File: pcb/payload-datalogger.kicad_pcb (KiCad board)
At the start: 2 copper layers, 50.5 x 41.5 mm, 39 parts, among them J1 2.54mm 01x02 header, J2 DE15 Socket, SW2 PTS815, U1 XIAO-ESP32-C3-DIP, U2 NCP177AMX330TCG, U3 W25X40CLSN, U4 MCP96RL00T-E_MX, U5 MCP96RL00T-E_MX, U6 MCP96RL00T-E_MX, U7 MCP96RL00T-E_MX

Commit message: Update payload-datalogger.kicad_pcb
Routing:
- net +3V3: track 18.5 -> 14.1 mm
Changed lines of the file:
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@@
 			(at -4.315 -2.77 90)
 			(layer "F.SilkS")
+			(hide yes)
 			(effects
 				(font
@@
 	)
 	(segment
-		(start 107.5 47.46)
-		(end 110.46 47.46)
-		(width 1)
-		(layer "F.Cu")
-		(net 3)
-	)
-	(segment
 		(start 84.5 67.85)
 		(end 84 67.85)
@@
 		(layer "F.Cu")
 		(net 3)
-	)
-	(segment
-		(start 107.5 47.46)
-		(end 106.04 47.46)
-		(width 1)
-		(layer "F.Cu")
-		(net 3)

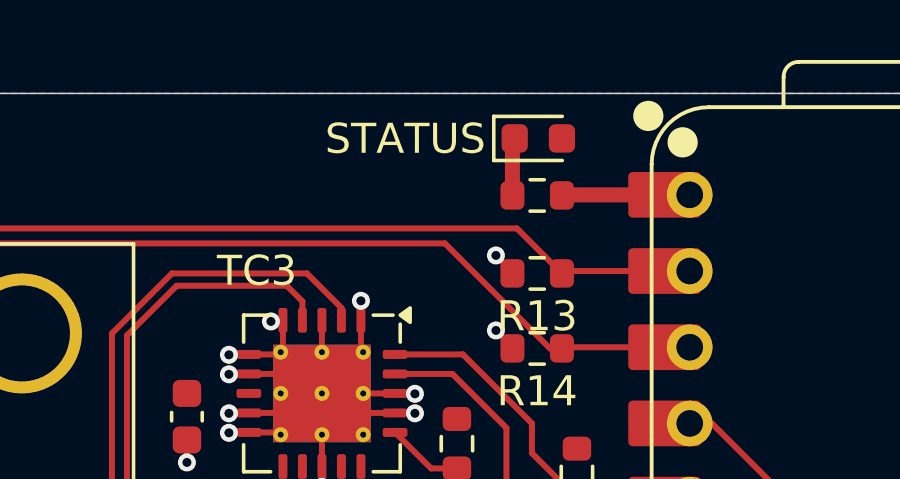
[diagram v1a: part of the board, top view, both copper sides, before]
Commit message: Add user button debounce to sch
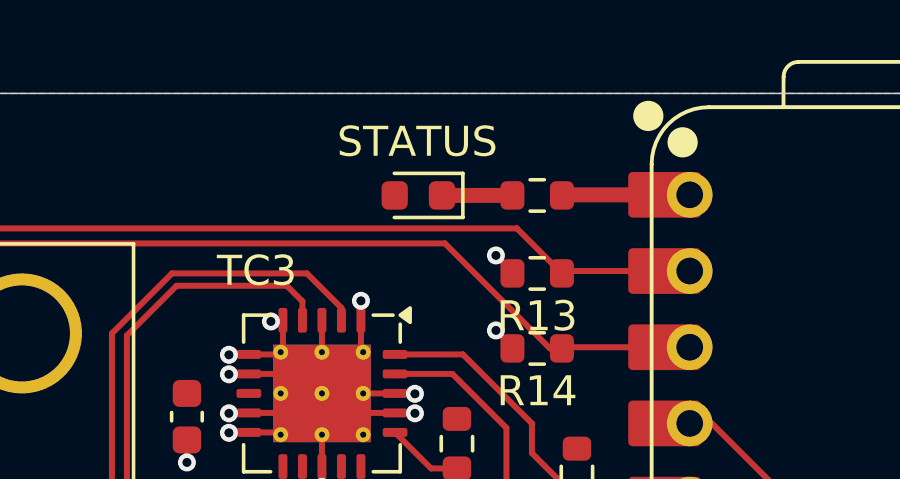
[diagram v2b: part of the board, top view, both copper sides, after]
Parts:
- moved D1 4.43 mm to (83.2, 42.4), turned to 180 degrees
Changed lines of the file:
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@@
 	(footprint "LED_SMD:LED_0603_1608Metric"
 		(layer "F.Cu")
-		(at 87.2125 40.5)
+		(at 83.2125 42.4 180)
 		(descr "LED SMD 0603 (1608 Metric), square (rectangular) end terminal, IPC_7351 nominal, (Body size source: http://www.tortai-tech.com/upload/download/2011102023233369053.pdf), generated with kicad-footprint-generator")
 		(tags "LED")
@@
 		)
 		(property "Datasheet" ""
-			(at 0 0 0)
+			(at 0 0 180)
 			(unlocked yes)
 			(layer "F.Fab")
@@
 		)
 		(property "Description" "Light emitting diode"
-			(at 0 0 0)
+			(at 0 0 180)
 			(unlocked yes)
 			(layer "F.Fab")
@@
 		)
 		(property "Sim.Pins" "1=K 2=A"
-			(at 0 0 0)
+			(at 0 0 180)
 			(unlocked yes)
 			(layer "F.Fab")
@@
 		(attr smd)
 		(fp_line
-			(start -1.485 -0.735)
-			(end -1.485 0.735)
+			(start 0.8 -0.735)
+			(end -1.485 -0.735)
 			(stroke
 				(width 0.12)
@@
 		)
 		(fp_line
-			(start 0.8 -0.735)
-			(end -1.485 -0.735)
+			(start -1.485 -0.735)
+			(end -1.485 0.735)
 			(stroke
 				(width 0.12)
@@
 		)
 		(fp_line
-			(start -1.48 -0.73)
-			(end 1.48 -0.73)
+			(start 1.48 0.73)
+			(end -1.48 0.73)
 			(stroke
 				(width 0.05)
@@
 		)
 		(fp_line
-			(start -1.48 0.73)
-			(end -1.48 -0.73)
+			(start 1.48 -0.73)
+			(end 1.48 0.73)
 			(stroke
 				(width 0.05)
@@
 		)
 		(fp_line
-			(start 1.48 -0.73)
-			(end 1.48 0.73)
+			(start -1.48 0.73)
+			(end -1.48 -0.73)
 			(stroke
 				(width 0.05)
@@
 		)
 		(fp_line
-			(start 1.48 0.73)
-			(end -1.48 0.73)
+			(start -1.48 -0.73)
+			(end 1.48 -0.73)
 			(stroke
 				(width 0.05)
@@
 		)
 		(fp_line
-			(start -0.8 -0.1)
-			(end -0.8 0.4)
+			(start 0.8 0.4)
+			(end 0.8 -0.4)
 			(stroke
 				(width 0.1)
@@
 		)
 		(fp_line
-			(start -0.8 0.4)
-			(end 0.8 0.4)
+			(start 0.8 -0.4)
+			(end -0.5 -0.4)
 			(stroke
 				(width 0.1)
@@
 		)
 		(fp_line
-			(start 0.8 -0.4)
-			(end -0.5 -0.4)
+			(start -0.8 0.4)
+			(end 0.8 0.4)
 			(stroke
 				(width 0.1)
@@
 		)
 		(fp_line
-			(start 0.8 0.4)
-			(end 0.8 -0.4)
+			(start -0.8 -0.1)
+			(end -0.8 0.4)
 			(stroke
 				(width 0.1)
@@
 		)
 		(pad "1" smd roundrect
-			(at -0.7875 0)
+			(at -0.7875 0 180)
 			(size 0.875 0.95)
 			(layers "F.Cu" "F.Mask" "F.Paste")
@@
 		)
 		(pad "2" smd roundrect
-			(at 0.7875 0)
+			(at 0.7875 0 180)
 			(size 0.875 0.95)
 			(layers "F.Cu" "F.Mask" "F.Paste")
@@
 	)
 	(gr_text "STATUS"
-		(at 80.1 41.1 0)
+		(at 80.5 41.2 0)
 		(layer "F.SilkS")
 		(effects
@@
 	)
 	(segment
-		(start 86.35 40.575)
-		(end 86.425 40.5)
-		(width 0.5)
-		(layer "F.Cu")
-		(net 6)
-	)
-	(segment
 		(start 86.35 42.4)
-		(end 86.35 40.575)
+		(end 84 42.4)
 		(width 0.5)
 		(layer "F.Cu")

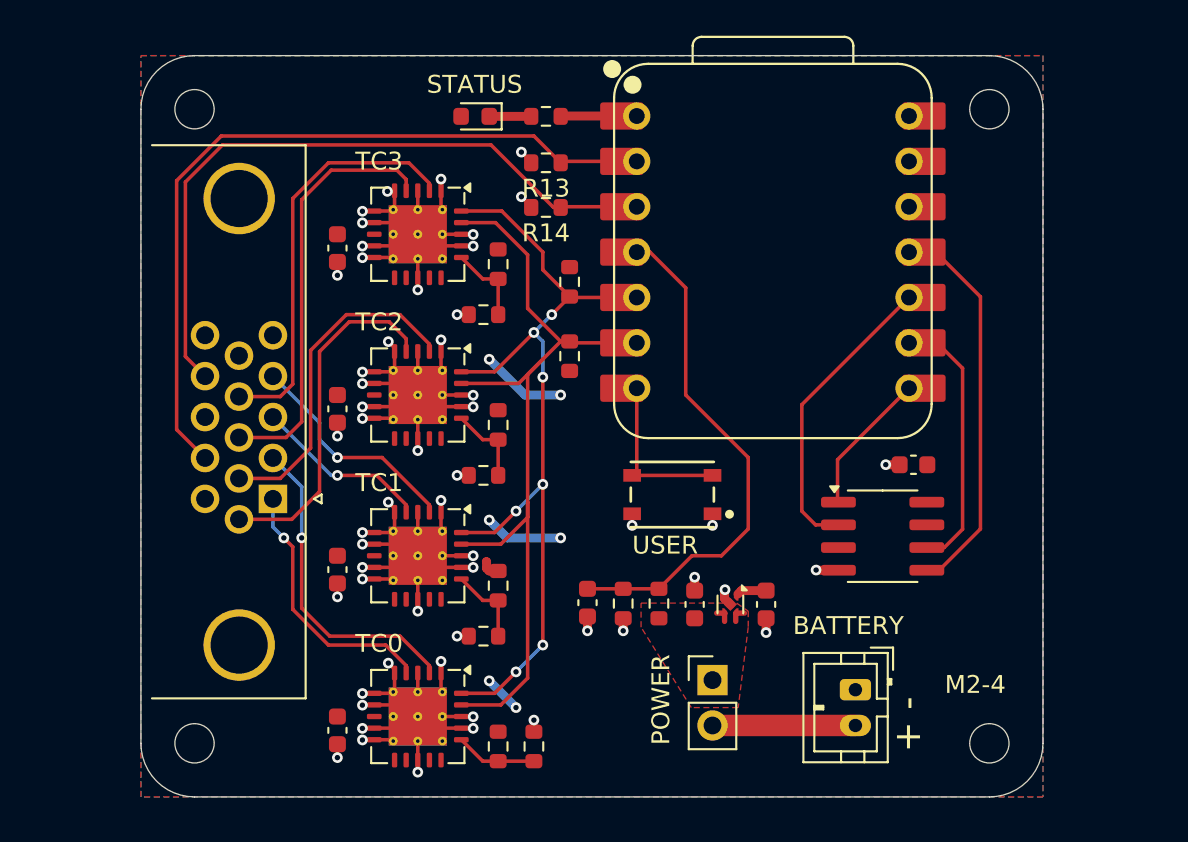
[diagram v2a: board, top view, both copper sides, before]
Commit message: Add PCB button debounce
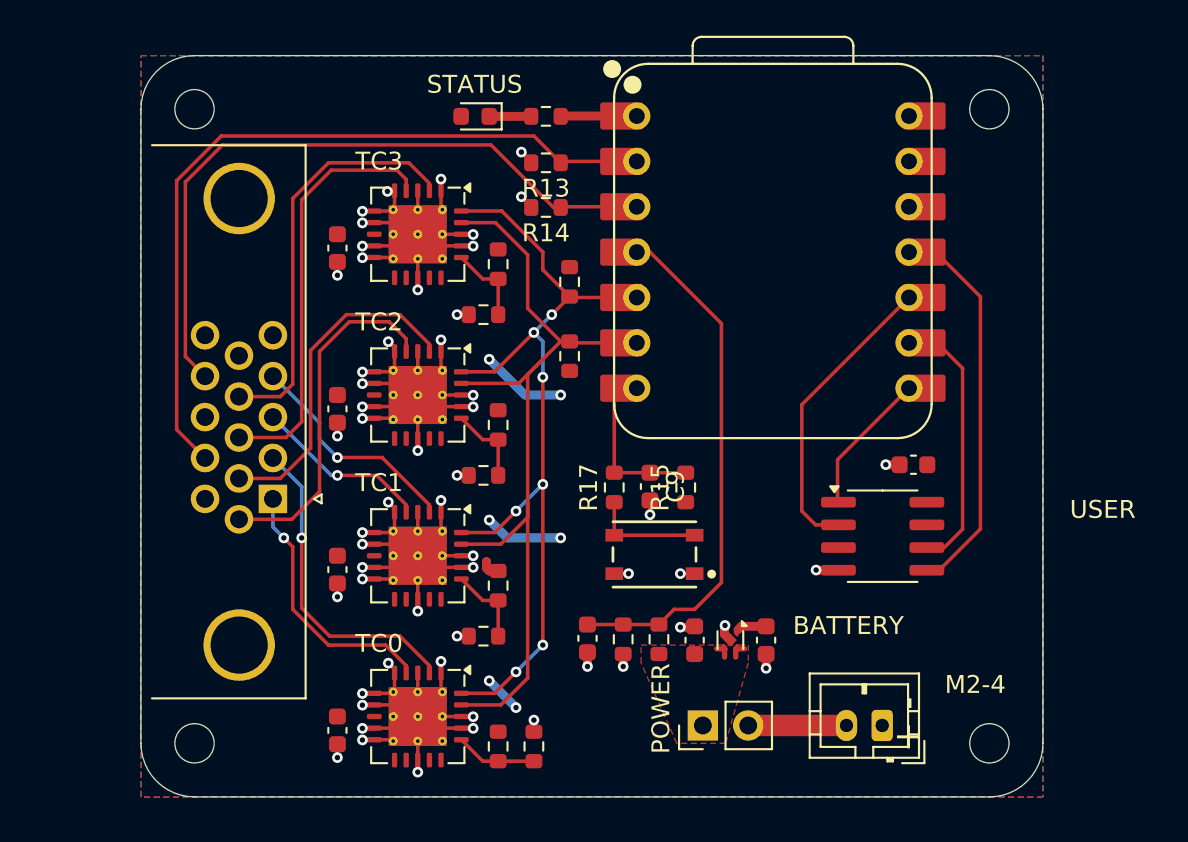
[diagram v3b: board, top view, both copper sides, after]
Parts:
- added C9: 1u, Capacitor_SMD:C_0603_1608Metric, F.Cu at (93.0, 63.1)
- added R15: 10k, Resistor_SMD:R_0603_1608Metric, F.Cu at (95.0, 63.2)
- added R17: 2.2k, Resistor_SMD:R_0603_1608Metric, F.Cu at (91.0, 63.2)
- moved SW2 3.50 mm to (93.2, 66.9)
- moved J1 2.60 mm to (96.0, 76.5), turned to 90 degrees
- moved BT1 2.50 mm to (106.0, 76.5), turned to 180 degrees
- moved C1 2.00 mm to (89.5, 71.6)
- moved C2 2.00 mm to (95.5, 71.7)
- moved C3 2.00 mm to (99.5, 71.7)
- moved R3 2.00 mm to (93.5, 71.7)
- moved R4 2.00 mm to (91.5, 71.7)
- moved U2 2.00 mm to (97.5, 71.7)
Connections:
- SW2 pad 2: Net-(U1-GPIO21/D6/TX) -> Net-(R17-Pad1)
- U1 pad 7: Net-(U1-GPIO21/D6/TX) -> /BUTTON
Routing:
- net Net-(U1-GPIO21/D6/TX): track 9.49 -> 0.00 mm
- net /BUTTON: track 0.00 -> 8.91 mm
- net Net-(R17-Pad1): track 0.00 -> 6.35 mm
- net Net-(BT1--): track 8.00 -> 5.50 mm
- net GND: track 132.9 -> 134.1 mm, vias 55 -> 56

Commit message: Move D-sub further out
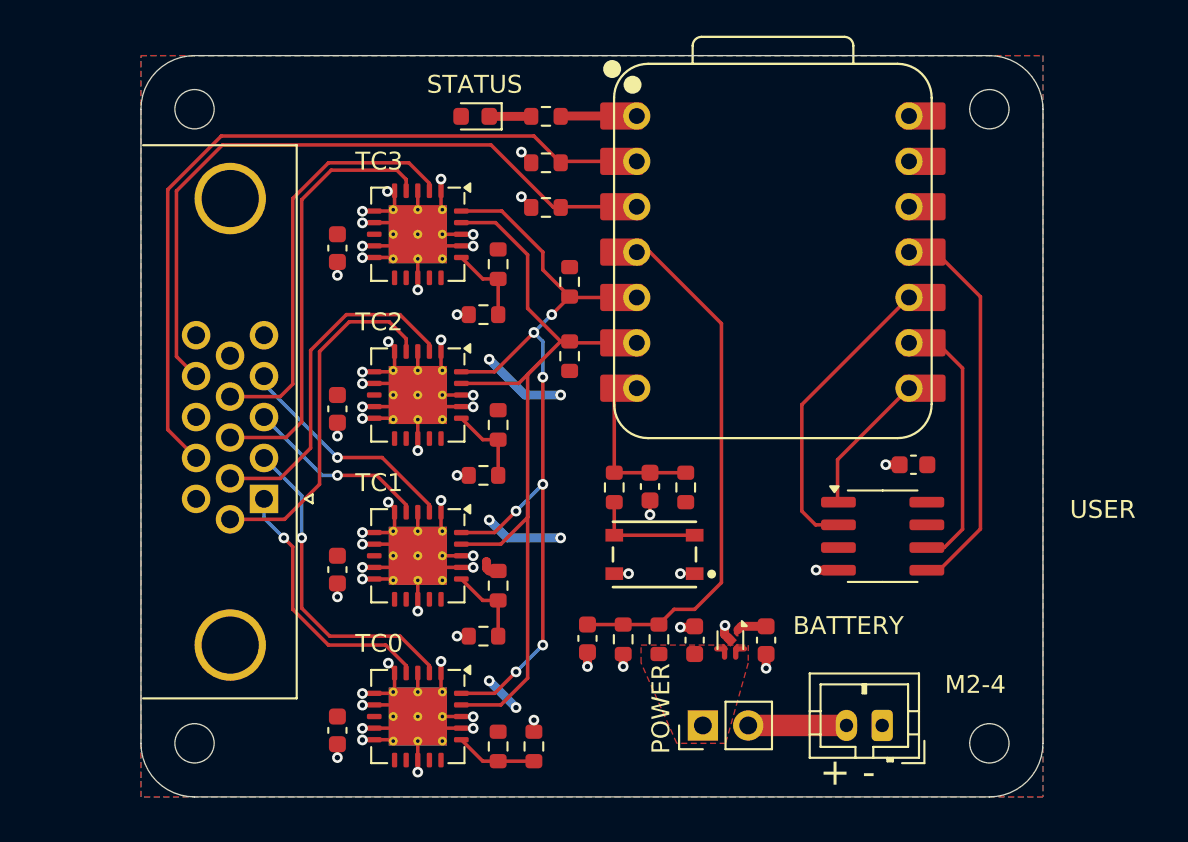
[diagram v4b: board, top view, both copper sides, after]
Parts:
- moved J2 0.50 mm to (71.4, 63.8)
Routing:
- net /TC3-: track 23.7 -> 24.2 mm
- net /TC3+: track 23.1 -> 23.6 mm
- net /TC2+: track 18.8 -> 19.3 mm
- net /TC1-: track 9.91 -> 10.4 mm
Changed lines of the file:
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@@
 			(at 0 -1.43 0)
 			(layer "F.SilkS")
+			(hide yes)
 			(effects
 				(font
@@
 			(at 0 -1.43 90)
 			(layer "F.SilkS")
+			(hide yes)
 			(effects
 				(font
@@
 			(at 0 -1.43 90)
 			(layer "F.SilkS")
+			(hide yes)
 			(effects
 				(font
@@
 			(at 0 -1.43 90)
 			(layer "F.SilkS")
+			(hide yes)
 			(effects
 				(font
@@
 			(at 0 -1.43 0)
 			(layer "F.SilkS")
+			(hide yes)
 			(effects
 				(font
@@
 	(footprint "Connector_Dsub:DSUB-15-HD_Socket_Horizontal_P2.29x1.90mm_EdgePinOffset3.03mm_Housed_MountingHolesOffset4.94mm"
 		(layer "F.Cu")
-		(at 71.89 63.815 -90)
+		(at 71.39 63.815 -90)
 		(descr "15-pin D-Sub connector, horizontal/angled (90 deg), THT-mount, socket (female), pitch 2.29x1.9mm, pin-PCB-offset 3.03mm, distance of mounting holes 25mm, distance of mounting holes to PCB edge 4.94mm, see https://disti-assets.s3.amazonaws.com/tonar/files/datasheets/16730.pdf")
 		(tags "15-pin D-Sub connector horizontal angled 90deg THT socket pitch 2.29x1.9mm pin-PCB-offset 3.03mm mounting-holes-distance 25mm mounting-hole-offset 4.94mm")
@@
 	)
 	(gr_text "+ -"
-		(at 108.3 78 90)
+		(at 102.5 80 0)
 		(layer "F.SilkS")
 		(effects
@@
 	)
 	(segment
-		(start 76.1661 53.901)
-		(end 78.401 53.901)
+		(start 72.54 64.96)
+		(end 69.49 64.96)
 		(width 0.2)
 		(layer "F.Cu")
@@
 	)
 	(segment
-		(start 78.401 53.901)
-		(end 79.35 54.85)
+		(start 76.1661 53.901)
+		(end 78.401 53.901)
 		(width 0.2)
 		(layer "F.Cu")
@@
 	)
 	(segment
-		(start 74.5 63.407)
-		(end 74.5 55.5671)
+		(start 78.401 53.901)
+		(end 79.35 54.85)
 		(width 0.2)
 		(layer "F.Cu")
@@
 	)
 	(segment
-		(start 72.947 64.96)
-		(end 74.5 63.407)
+		(start 74.5 63)
+		(end 74.5 55.5671)
 		(width 0.2)
 		(layer "F.Cu")
@@
 	)
 	(segment
-		(start 69.99 64.96)
-		(end 72.947 64.96)
+		(start 74.5 63)
+		(end 72.54 64.96)
 		(width 0.2)
 		(layer "F.Cu")
@@
 	)
 	(segment
-		(start 71.89 56.945)
-		(end 74.5 59.555)
+		(start 71.39 57.39)
+		(end 71.39 56.945)
 		(width 0.2)
 		(layer "B.Cu")
@@
 	)
 	(segment
-		(start 74.5 59.555)
-		(end 74.5 60.5)
+		(start 75.5 61.5)
+		(end 71.39 57.39)
 		(width 0.2)
 		(layer "B.Cu")
@@
 	)
 	(segment
-		(start 74.5 60.5)
-		(end 75.5 61.5)
+		(start 88.08 44.92)
+		(end 88 45)
 		(width 0.2)
-		(layer "B.Cu")
-		(net 8)
+		(layer "F.Cu")
+		(net 9)
 	)
 	(segment
@@
 	)
 	(segment
-		(start 69 43.5)
-		(end 66.5 46)
+		(start 66 59.935)
+		(end 67.59 61.525)
 		(width 0.2)
 		(layer "F.Cu")
@@
 	)
 	(segment
-		(start 88.08 44.92)
-		(end 88 45)
+		(start 86.5 43.5)
+		(end 69 43.5)
 		(width 0.2)
 		(layer "F.Cu")
@@
 	)
 	(segment
-		(start 66.5 46)
-		(end 66.5 59.935)
+		(start 66 46.5)
+		(end 66 59.935)
 		(width 0.2)
 		(layer "F.Cu")
@@
 	)
 	(segment
-		(start 86.5 43.5)
-		(end 69 43.5)
-		(width 0.2)
-		(layer "F.Cu")
-		(net 9)
-	)
-	(segment
-		(start 66.5 59.935)
-		(end 68.09 61.525)
+		(start 91.425 44.92)
+		(end 88.08 44.92)
 		(width 0.2)
 		(layer "F.Cu")
@@
 	)
 	(segment
-		(start 91.425 44.92)
-		(end 88.08 44.92)
+		(start 69 43.5)
+		(end 66 46.5)
 		(width 0.2)
 		(layer "F.Cu")
@@
 	)
 	(segment
-		(start 71.89 65.39)
-		(end 71.89 63.815)
+		(start 72.5 66)
+		(end 71.39 64.89)
 		(width 0.2)
 		(layer "B.Cu")
@@
 	)
 	(segment
-		(start 72.5 66)
-		(end 71.89 65.39)
+		(start 71.39 64.89)
+		(end 71.39 63.815)
 		(width 0.2)
 		(layer "B.Cu")
@@
 	(segment
 		(start 73.5 59.5)
-		(end 73.5 47.0671)
+		(end 72.62 60.38)
 		(width 0.2)
 		(layer "F.Cu")
@@
 	)
 	(segment
-		(start 78.827866 45.410765)
-		(end 79.35 45.932899)
+		(start 72.62 60.38)
+		(end 69.49 60.38)
 		(width 0.2)
 		(layer "F.Cu")
@@
 	)
 	(segment
-		(start 79.35 45.932899)
-		(end 79.35 46.5625)
+		(start 73.5 59.5)
+		(end 73.5 47.0671)
 		(width 0.2)
 		(layer "F.Cu")
@@
 	)
 	(segment
-		(start 75.156335 45.410765)
-		(end 78.827866 45.410765)
+		(start 78.827866 45.410765)
+		(end 79.35 45.932899)
 		(width 0.2)
 		(layer "F.Cu")
@@
 	)
 	(segment
-		(start 72.62 60.38)
-		(end 73.5 59.5)
+		(start 79.35 45.932899)
+		(end 79.35 46.5625)
 		(width 0.2)
 		(layer "F.Cu")
@@
 	)
 	(segment
-		(start 69.99 60.38)
-		(end 72.62 60.38)
+		(start 75.156335 45.410765)
+		(end 78.827866 45.410765)
 		(width 0.2)
 		(layer "F.Cu")
@@
 	)
 	(segment
-		(start 73.5 69.9329)
-		(end 75.0671 71.5)
+		(start 80.65 73.150001)
+		(end 80.65 73.5625)
 		(width 0.2)
 		(layer "F.Cu")
@@
 	)
 	(segment
-		(start 75.0671 71.5)
-		(end 78.999999 71.5)
+		(start 73.5 66)
+		(end 73.5 69.9329)
 		(width 0.2)
 		(layer "F.Cu")
@@
 	)
 	(segment
-		(start 73.5 66)
-		(end 73.5 69.9329)
+		(start 75.0671 71.5)
+		(end 78.999999 71.5)
 		(width 0.2)
 		(layer "F.Cu")
@@
 	)
 	(segment
-		(start 78.999999 71.5)
-		(end 80.65 73.150001)
+		(start 73.5 69.9329)
+		(end 75.0671 71.5)
 		(width 0.2)
 		(layer "F.Cu")
@@
 	)
 	(segment
-		(start 80.65 73.150001)
-		(end 80.65 73.5625)
+		(start 78.999999 71.5)
+		(end 80.65 73.150001)
 		(width 0.2)
 		(layer "F.Cu")
@@
 	)
 	(segment
-		(start 73.5 63.135)
-		(end 71.89 61.525)
+		(start 73.5 66)
+		(end 73.5 63.635)
 		(width 0.2)
 		(layer "B.Cu")
@@
 	)
 	(segment
-		(start 73.5 66)
-		(end 73.5 63.135)
+		(start 73.5 63.635)
+		(end 71.39 61.525)
 		(width 0.2)
 		(layer "B.Cu")
@@
 	)
 	(segment
-		(start 69.99 62.67)
-		(end 72.30205 62.67)
+		(start 74 55.5)
+		(end 76 53.5)
 		(width 0.2)
 		(layer "F.Cu")
@@
 	)
 	(segment
-		(start 72.30205 62.67)
-		(end 74 60.97205)
+		(start 74 60.97205)
+		(end 74 55.5)
 		(width 0.2)
 		(layer "F.Cu")
@@
 	)
 	(segment
-		(start 74 55.5)
-		(end 76 53.5)
+		(start 76 53.5)
+		(end 78.999999 53.5)
 		(width 0.2)
 		(layer "F.Cu")
@@
 	(segment
 		(start 74 60.97205)
-		(end 74 55.5)
+		(end 72.30205 62.67)
 		(width 0.2)
 		(layer "F.Cu")
@@
 	)
 	(segment
-		(start 76 53.5)
-		(end 78.999999 53.5)
+		(start 80.65 55.150001)
+		(end 80.65 55.5625)
 		(width 0.2)
 		(layer "F.Cu")
@@
 	)
 	(segment
-		(start 80.65 55.150001)
-		(end 80.65 55.5625)
+		(start 78.999999 53.5)
+		(end 80.65 55.150001)
 		(width 0.2)
 		(layer "F.Cu")
@@
 	)
 	(segment
-		(start 78.999999 53.5)
-		(end 80.65 55.150001)
+		(start 72.30205 62.67)
+		(end 69.49 62.67)
 		(width 0.2)
 		(layer "F.Cu")
@@
 	)
 	(segment
-		(start 72.30205 58.09)
-		(end 73 57.39205)
+		(start 73 57.39205)
+		(end 72.30205 58.09)
 		(width 0.2)
 		(layer "F.Cu")
@@
 	)
 	(segment
-		(start 69.99 58.09)
-		(end 72.30205 58.09)
+		(start 72.30205 58.09)
+		(end 69.49 58.09)
 		(width 0.2)
 		(layer "F.Cu")
@@
 	)
 	(segment
-		(start 87.6 47.5)
-		(end 84.1 44)
+		(start 69.0671 44)
+		(end 66.489 46.5781)
 		(width 0.2)
 		(layer "F.Cu")
@@
 	)
 	(segment
-		(start 66.989 46.0781)
-		(end 66.989 55.844)
+		(start 88.04 47.46)
+		(end 88 47.5)
 		(width 0.2)
 		(layer "F.Cu")
@@
 	)
 	(segment
-		(start 69.0671 44)
-		(end 66.989 46.0781)
+		(start 91.425 47.46)
+		(end 88.04 47.46)
 		(width 0.2)
 		(layer "F.Cu")
@@
 	)
 	(segment
-		(start 88.04 47.46)
-		(end 88 47.5)
+		(start 84.1 44)
+		(end 69.0671 44)
 		(width 0.2)
 		(layer "F.Cu")
@@
 	)
 	(segment
-		(start 91.425 47.46)
-		(end 88.04 47.46)
+		(start 87.6 47.5)
+		(end 84.1 44)
 		(width 0.2)
 		(layer "F.Cu")
@@
 	)
 	(segment
-		(start 66.989 55.844)
-		(end 68.09 56.945)
+		(start 66.489 46.5781)
+		(end 66.489 55.844)
 		(width 0.2)
 		(layer "F.Cu")
@@
 	)
 	(segment
-		(start 84.1 44)
-		(end 69.0671 44)
+		(start 66.489 55.844)
+		(end 67.59 56.945)
 		(width 0.2)
 		(layer "F.Cu")
@@
 	)
 	(segment
-		(start 71.89 59.235)
-		(end 75.155 62.5)
+		(start 74.655 62.5)
+		(end 75.5 62.5)
 		(width 0.2)
 		(layer "B.Cu")
@@
 	)
 	(segment
-		(start 75.155 62.5)
-		(end 75.5 62.5)
+		(start 71.39 59.235)
+		(end 74.655 62.5)
 		(width 0.2)
 		(layer "B.Cu")
